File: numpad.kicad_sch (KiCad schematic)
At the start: 0 parts

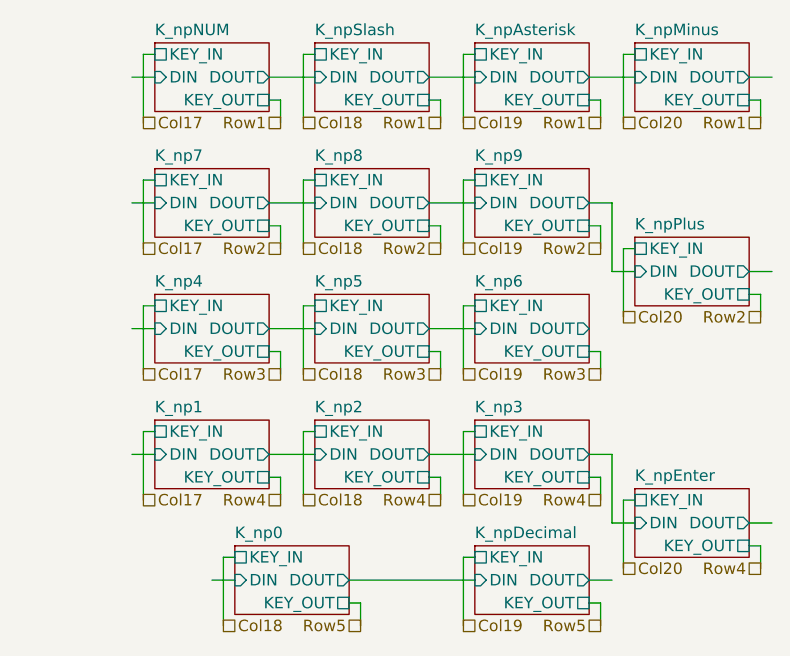
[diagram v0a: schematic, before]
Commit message: Unified key sch pages
One large page is simpler in this case
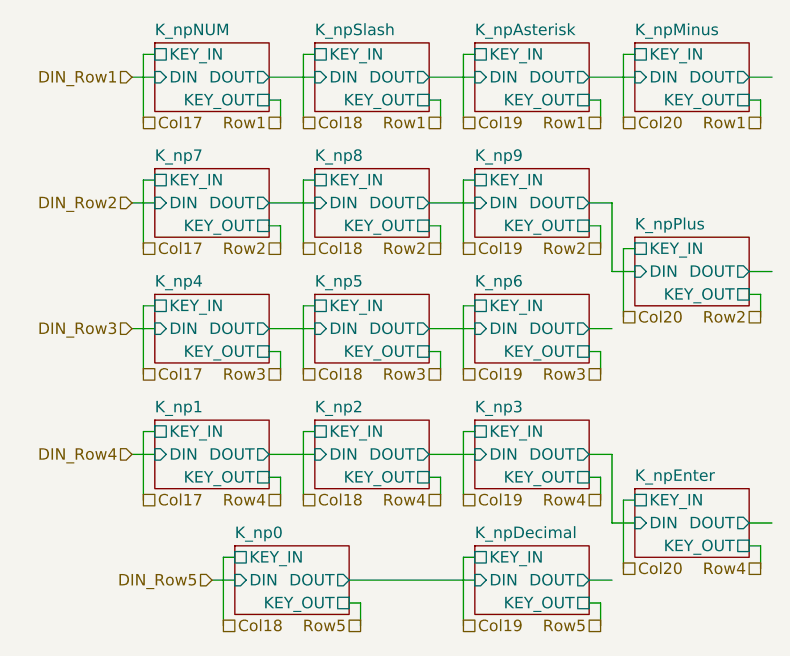
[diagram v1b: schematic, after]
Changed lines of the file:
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@@
+	(wire
+		(pts
+			(xy 166.37 99.06) (xy 168.91 99.06)
+		)
+		(stroke
+			(width 0)
+			(type default)
+		)
+	)
 	(wire
 		(pts
@@
 		)
 	)
+	(hierarchical_label "DIN_Row2"
+		(shape input)
+		(at 115.57 85.09 180)
+		(effects
+			(font
+				(size 1.27 1.27)
+			)
+			(justify right)
+		)
+	)
+	(hierarchical_label "DIN_Row5"
+		(shape input)
+		(at 124.46 127 180)
+		(effects
+			(font
+				(size 1.27 1.27)
+			)
+			(justify right)
+		)
+	)
 	(hierarchical_label "Col19"
 		(shape passive)
@@
 		)
 	)
+	(hierarchical_label "DIN_Row4"
+		(shape input)
+		(at 115.57 113.03 180)
+		(effects
+			(font
+				(size 1.27 1.27)
+			)
+			(justify right)
+		)
+	)
 	(hierarchical_label "Row4"
 		(shape passive)
@@
 		)
 	)
+	(hierarchical_label "DIN_Row3"
+		(shape input)
+		(at 115.57 99.06 180)
+		(effects
+			(font
+				(size 1.27 1.27)
+			)
+			(justify right)
+		)
+	)
 	(hierarchical_label "Col19"
 		(shape passive)
@@
 		)
 	)
+	(hierarchical_label "DIN_Row1"
+		(shape input)
+		(at 115.57 71.12 180)
+		(effects
+			(font
+				(size 1.27 1.27)
+			)
+			(justify right)
+		)
+	)
